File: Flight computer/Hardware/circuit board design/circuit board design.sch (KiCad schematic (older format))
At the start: 0 parts

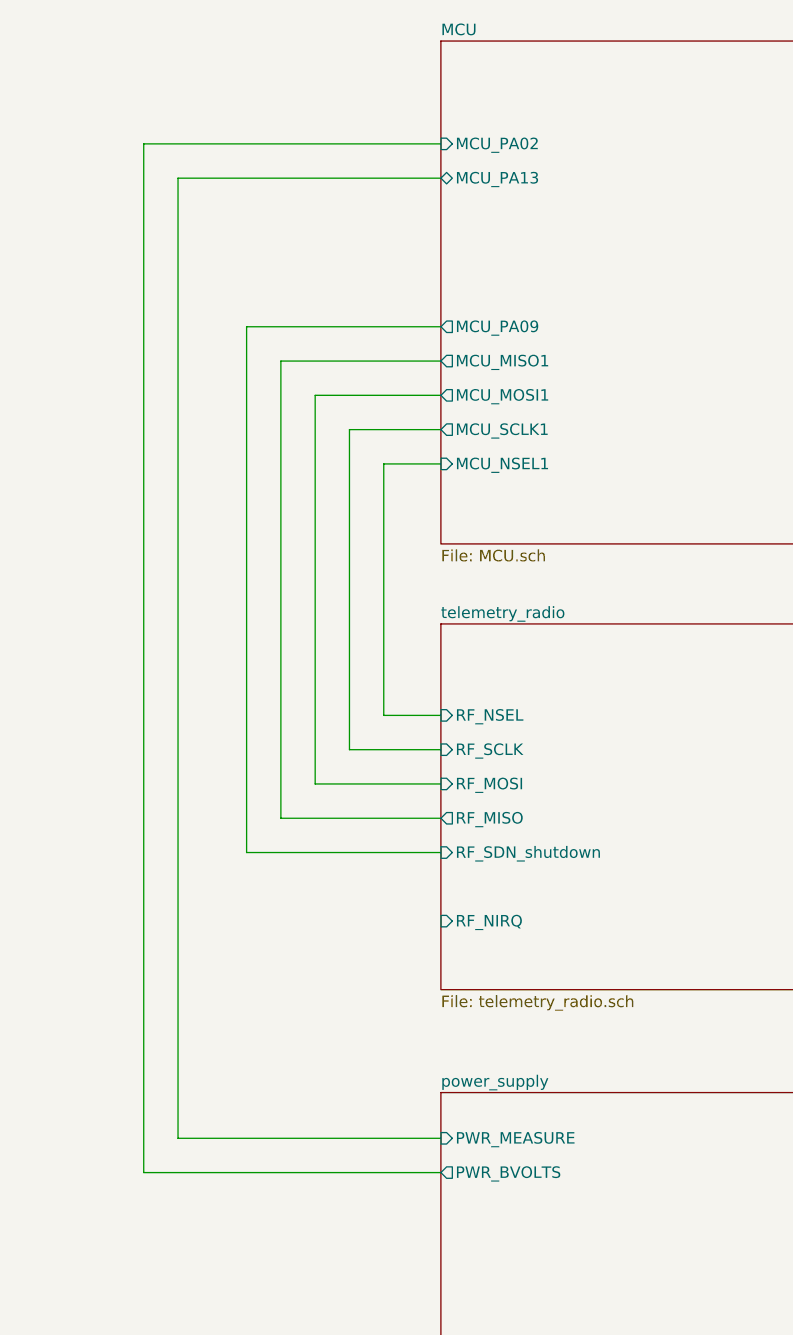
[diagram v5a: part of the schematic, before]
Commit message: Work in progress for Telemetry Radio
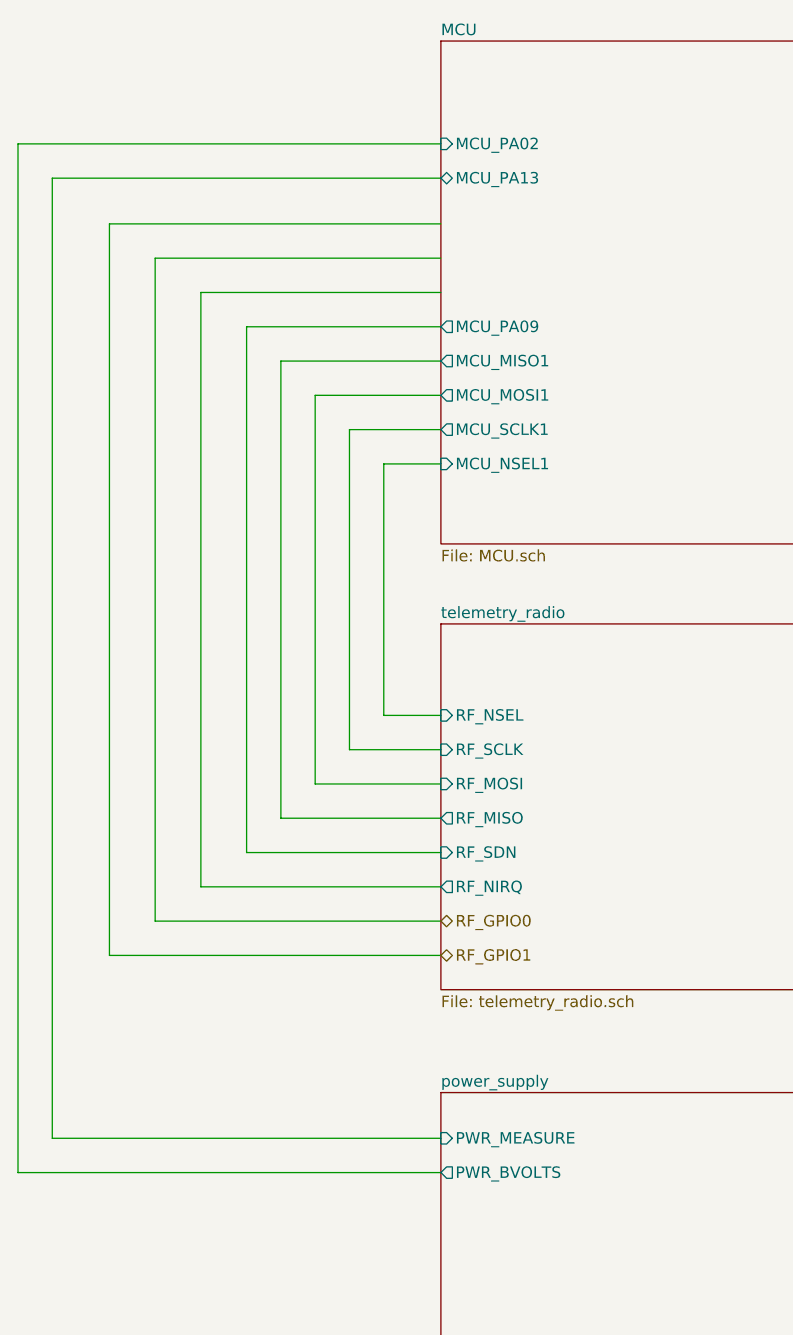
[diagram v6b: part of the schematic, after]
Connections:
- net labels added: RF_GPIO0, RF_GPIO1
- wire segments 34 -> 43
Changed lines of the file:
@@
 $EndSheet
 Wire Wire Line
-	2700 1550 1400 1550
+	2700 1550 850  1550
 Wire Wire Line
-	1400 1550 1400 6050
+	850  1550 850  6050
 Wire Wire Line
-	1400 6050 2700 6050
+	850  6050 2700 6050
 Wire Wire Line
-	2700 1700 1550 1700
+	2700 1700 1000 1700
 Wire Wire Line
-	1550 1700 1550 5900
+	1000 1700 1000 5900
 Wire Wire Line
-	1550 5900 2700 5900
+	1000 5900 2700 5900
 Wire Wire Line
 	2000 2500 2700 2500
@@
 Wire Wire Line
 	2450 2950 2450 4050
+Wire Wire Line
+	2700 4650 1850 4650
+Wire Wire Line
+	1850 2350 2700 2350
+Wire Wire Line
+	1850 2350 1850 4650
 $Sheet
 S 2700 3650 2350 1600
@@
 F4 "RF_MOSI" I L 2700 4350 50
 F5 "RF_NSEL" I L 2700 4050 50
-F6 "RF_SDN_shutdown" I L 2700 4650 50
-F7 "RF_NIRQ" I L 2700 4950 50
+F6 "RF_SDN" I L 2700 4650 50
+F7 "RF_NIRQ" O L 2700 4800 50
 $EndSheet
+Text HLabel 2700 4950 2    50   BiDi ~ 0
+RF_GPIO0
+Text HLabel 2700 5100 2    50   BiDi ~ 0
+RF_GPIO1
 Wire Wire Line
-	2700 4650 1850 4650
+	2700 4800 1650 4800
 Wire Wire Line
-	1850 2350 2700 2350
+	1650 4800 1650 2200
 Wire Wire Line
-	1850 2350 1850 4650
+	1650 2200 2700 2200
+Wire Wire Line
+	2700 4950 1450 4950
+Wire Wire Line
+	1450 4950 1450 2050
+Wire Wire Line
+	1450 2050 2700 2050
+Wire Wire Line
+	2700 5100 1250 5100
+Wire Wire Line
+	1250 5100 1250 1900
+Wire Wire Line
+	1250 1900 2700 1900
 $EndSCHEMATC

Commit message: changed the SPI flash chip
-changed to Winbond W74M64FV 64Mbit flash chip to run on 3.3V. Changed schematic symbol and foot print.
- changed the names of hierarchical labels for the pyros
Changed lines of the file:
@@
 F0 "pyro_driver" 50
 F1 "pyro_driver.sch" 50
-F2 "sense_fet_a" O L 7950 5200 50
-F3 "fire_a" O L 7950 5350 50
+F2 "SENSE_FET_A" O L 7950 5350 50
+F3 "FIRE_A" O L 7950 5500 50
 $EndSheet
 Wire Wire Line

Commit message: Wired the GYRO Ready and ACCL ready interrupt pins
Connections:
- wire segments 43 -> 49
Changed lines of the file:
@@
 F2 "SENS_SDA" B L 7900 3550 50
 F3 "SENS_SCL" B L 7900 3700 50
+F4 "ACCL_RDY" I L 7900 3900 50
+F5 "GYRO_RDY" I L 7900 4050 50
 $EndSheet
 $Sheet
@@
 F20 "MCU_PB02" O R 5050 1600 50
 F21 "MCU_PB08" I R 5050 2200 50
+F22 "MCU_PA20" I L 2700 1900 50
+F23 "MCU_PA21" I L 2700 2050 50
+F24 "MCU_PA27" I L 2700 2200 50
 $EndSheet
 Wire Wire Line
@@
 Wire Wire Line
 	1250 1900 2700 1900
+Wire Wire Line
+	7900 3900 6950 3900
+Wire Wire Line
+	6950 3900 6950 2400
+Wire Wire Line
+	6950 2400 5050 2400
+Wire Wire Line
+	7900 4050 6750 4050
+Wire Wire Line
+	6750 4050 6750 2550
+Wire Wire Line
+	6750 2550 5050 2550
 $EndSCHEMATC
